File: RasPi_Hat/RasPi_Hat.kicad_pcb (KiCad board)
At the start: 2 copper layers, 54.9 x 14.8 mm, 3 parts, among them J1 Fan, J2 Arduino Serial, J3 Pi Header

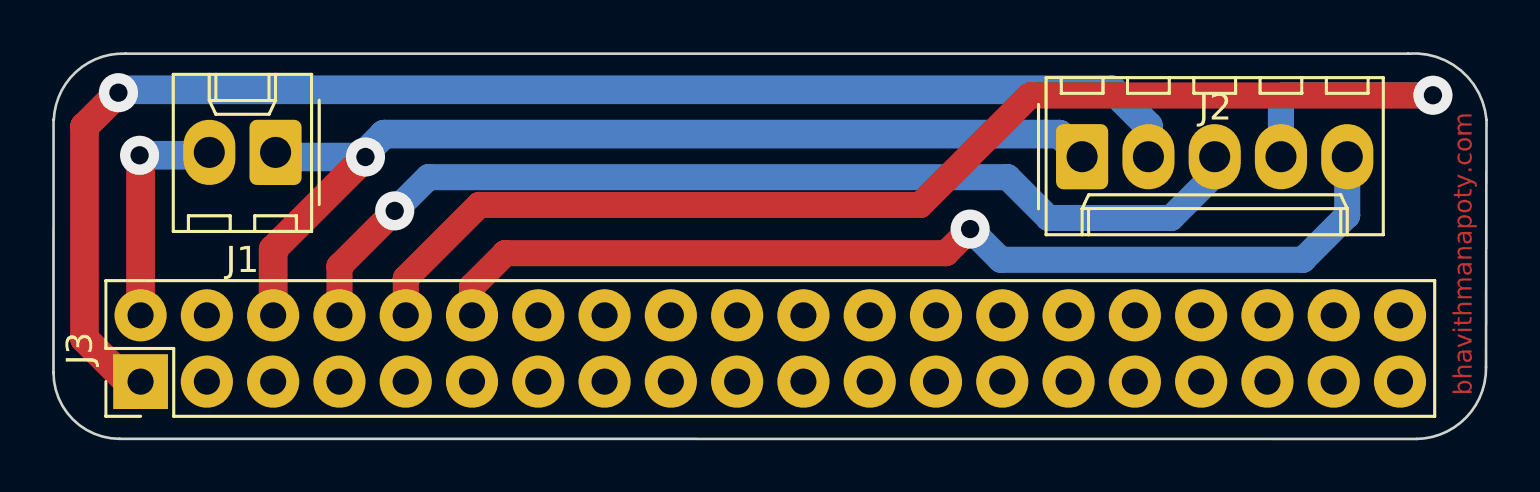
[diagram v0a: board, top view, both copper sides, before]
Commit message: Fixed Silkscreen
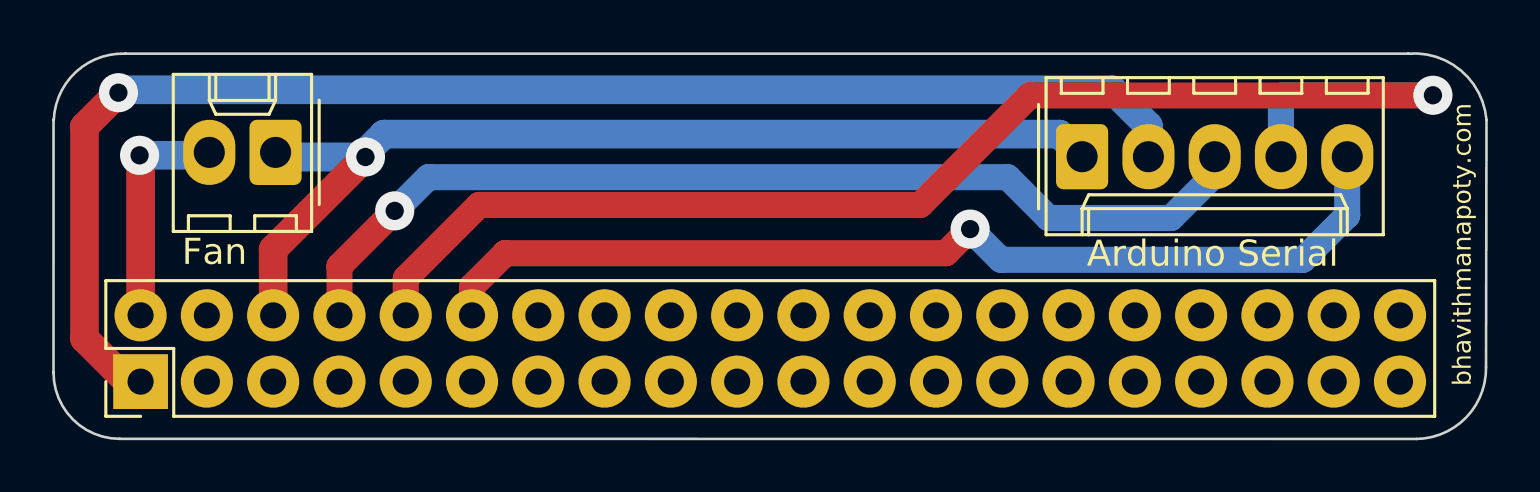
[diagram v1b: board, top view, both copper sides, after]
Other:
- board text added: "Arduino Serial"
- board text added: "Fan"
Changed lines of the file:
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@@
     (property "Sheetname" "")
     (attr through_hole)
-    (fp_text reference "J2" (at 5.101 -1.89) (layer "F.SilkS")
-      (effects (font (size 1 1) (thickness 0.15)))
-    )
-    (fp_text value "Arduino Serial" (at 5.08 4.08) (layer "F.Fab")
+    (fp_text reference "J2" (at 5.101 -1.89) (layer "F.SilkS") hide
+      (effects (font (size 1 1) (thickness 0.15)))
+    )
+    (fp_text value "Arduino Serial" (at 5.08 4.08) (layer "F.Fab") hide
       (effects (font (size 1 1) (thickness 0.15)))
     )
@@
     (property "Sheetname" "")
     (attr through_hole)
-    (fp_text reference "J1" (at 1.27 -4.12) (layer "F.SilkS")
-      (effects (font (size 1 1) (thickness 0.15)))
-    )
-    (fp_text value "Fan" (at 1.249 1.85) (layer "F.Fab")
+    (fp_text reference "J1" (at 13.394 -5.552) (layer "F.SilkS") hide
+      (effects (font (size 1 1) (thickness 0.15)))
+    )
+    (fp_text value "Fan" (at 1.201 -3.941) (layer "F.Fab") hide
       (effects (font (size 1 1) (thickness 0.15)))
     )
@@
     (property "Sheetname" "")
     (attr through_hole)
-    (fp_text reference "J3" (at 1.27 -2.33 90) (layer "F.SilkS")
+    (fp_text reference "J3" (at 1.27 -2.33 90) (layer "F.SilkS") hide
       (effects (font (size 1 1) (thickness 0.15)))
     )
@@
   (gr_arc (start 126.321 54.77) (mid 127.169949 52.930456) (end 129.071 52.23) (layer "Edge.Cuts") (width 0.1))
   (gr_line (start 178.543949 66.993949) (end 128.85 66.99) (layer "Edge.Cuts") (width 0.1))
-  (gr_text "bhavithmanapoty.com" (at 180.324 59.899 90) (layer "F.Cu")
+  (gr_text "bhavithmanapoty.com" (at 180.292 59.543 90) (layer "F.SilkS")
     (effects (font (size 0.7 0.7) (thickness 0.1)))
   )
+  (gr_text "Fan\n" (at 132.478 59.822) (layer "F.SilkS")
+    (effects (font (size 1 1) (thickness 0.15)))
+  )
+  (gr_text "Arduino Serial" (at 170.727 59.892) (layer "F.SilkS")
+    (effects (font (size 1 1) (thickness 0.15)))
+  )
   (segment (start 134.727 62.257) (end 134.727 59.727) (width 1.1) (layer "F.Cu") (net 1))
